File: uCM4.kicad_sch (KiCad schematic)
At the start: 74 parts, among them IC1 MAX17048G+, J1 Conn_02x07_Odd_Even, J10 USB_C_Receptacle, J11 SolderJumper_2_Open, J12 Conn_02x08_Odd_Even, J2 Micro_SD_Card_Det, J3 Conn_01x04, J4 Conn_01x04, J5 DummyJ, J6 DummyJ, J7 SolderJumper_2_Open, J8 Camera 0, J9 Camera 1, SW1 SW_DIP_x01, SW2 SW_DIP_x01, SW3 SW_Push, SW4 SW_Push, U1 BNO055, U18 RT9742GGJ5, U2 SN74LVC1G07DBVR, U3 TPD4EUSB30DQAR, U4 TPS61022, U5 BME690

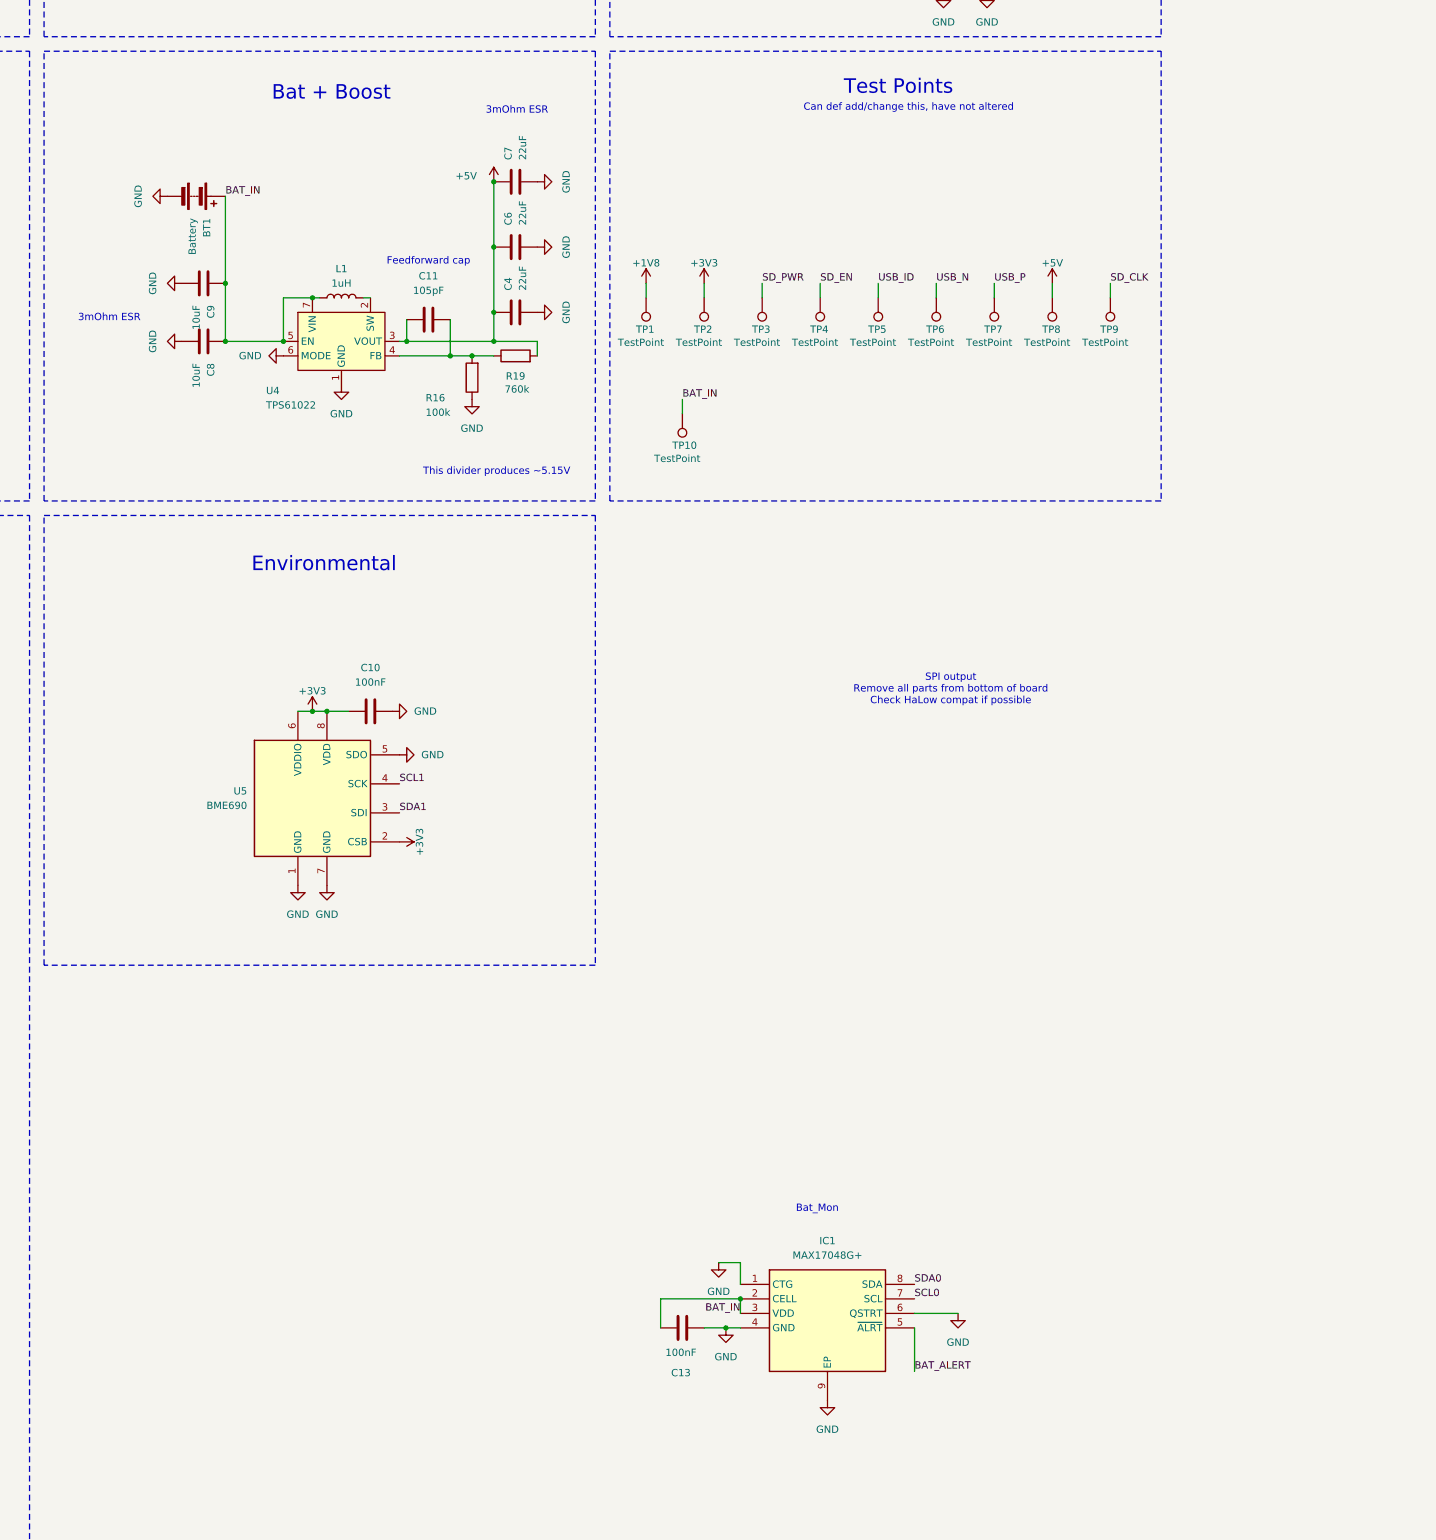
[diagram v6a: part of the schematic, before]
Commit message: Adding battery charging circuitry.
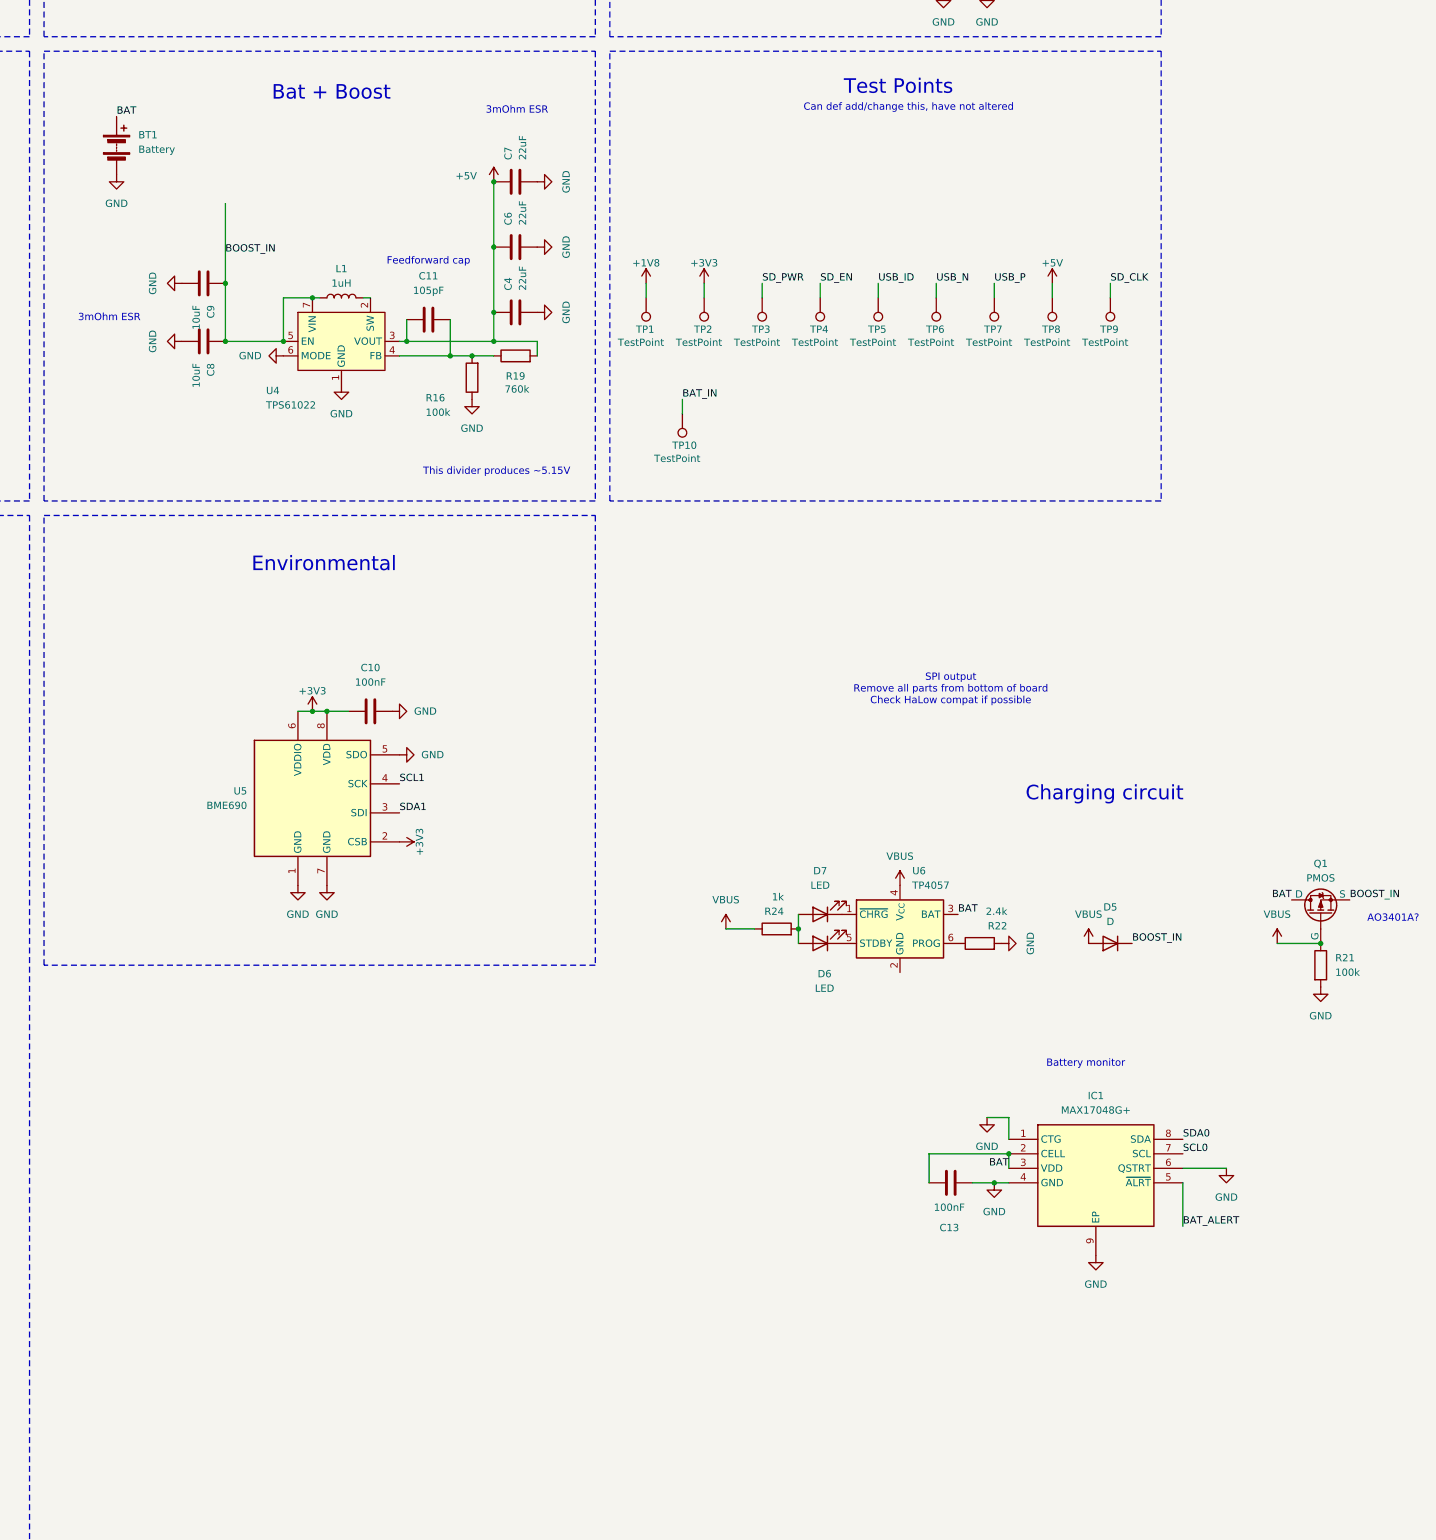
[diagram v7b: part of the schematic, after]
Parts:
- added D5: D, symbol Device:D
- added D6, D7: LED, symbol Device:LED
- added Q1: PMOS, symbol Simulation_SPICE:PMOS
- added R21: 100k, symbol Device:R
- added R22: 2.4k, symbol Device:R
- added R24: 1k, symbol Device:R
- added U6: TP4057, Package_TO_SOT_SMD:TSOT-23-6, symbol Battery_Management:TP4057
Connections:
- net BAT_IN: no longer BT1.1 (+), C13.1, C8.1, C9.1, IC1.2 (CELL), IC1.3 (VDD), L1.1, U4.5 (EN), U4.7 (VIN)
- net GND: now also R21.2, R22.2
- net VBUS: now also D5.2 (A), Q1.2 (G), R21.1, R24.1, U6.4 (V_{CC})
- new net: D6.2 (A), D7.2 (A), R24.2
- new net: R22.1, U6.6 (PROG)
- new net: D7.1 (K), U6.1 (~{CHRG})
- new net: D6.1 (K), U6.5 (STDBY)
- new net BAT: BT1.1 (+), C13.1, IC1.2 (CELL), IC1.3 (VDD), Q1.1 (D), U6.3 (BAT)
- new net BOOST_IN: C8.1, C9.1, D5.1 (K), L1.1, Q1.3 (S), U4.5 (EN), U4.7 (VIN)
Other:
- note added: "AO3401A?"
- note added: "Battery monitor"
- note added: "Charging circuit"
- note removed: "Bat_Mon"
- moved on the sheet: BT1, C13, IC1

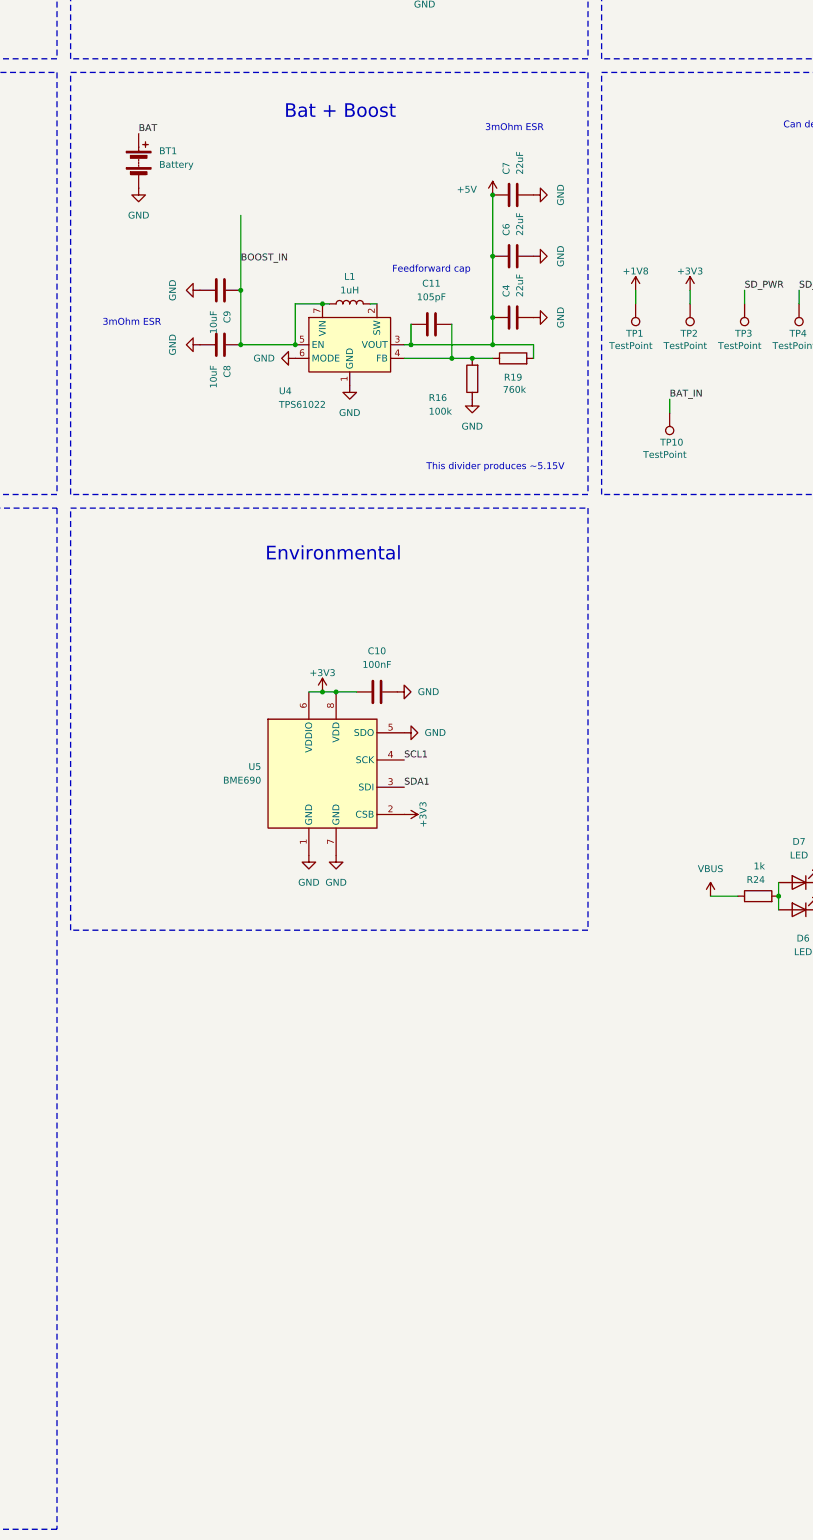
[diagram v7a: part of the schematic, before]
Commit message: Removing onboard environmental sensor.
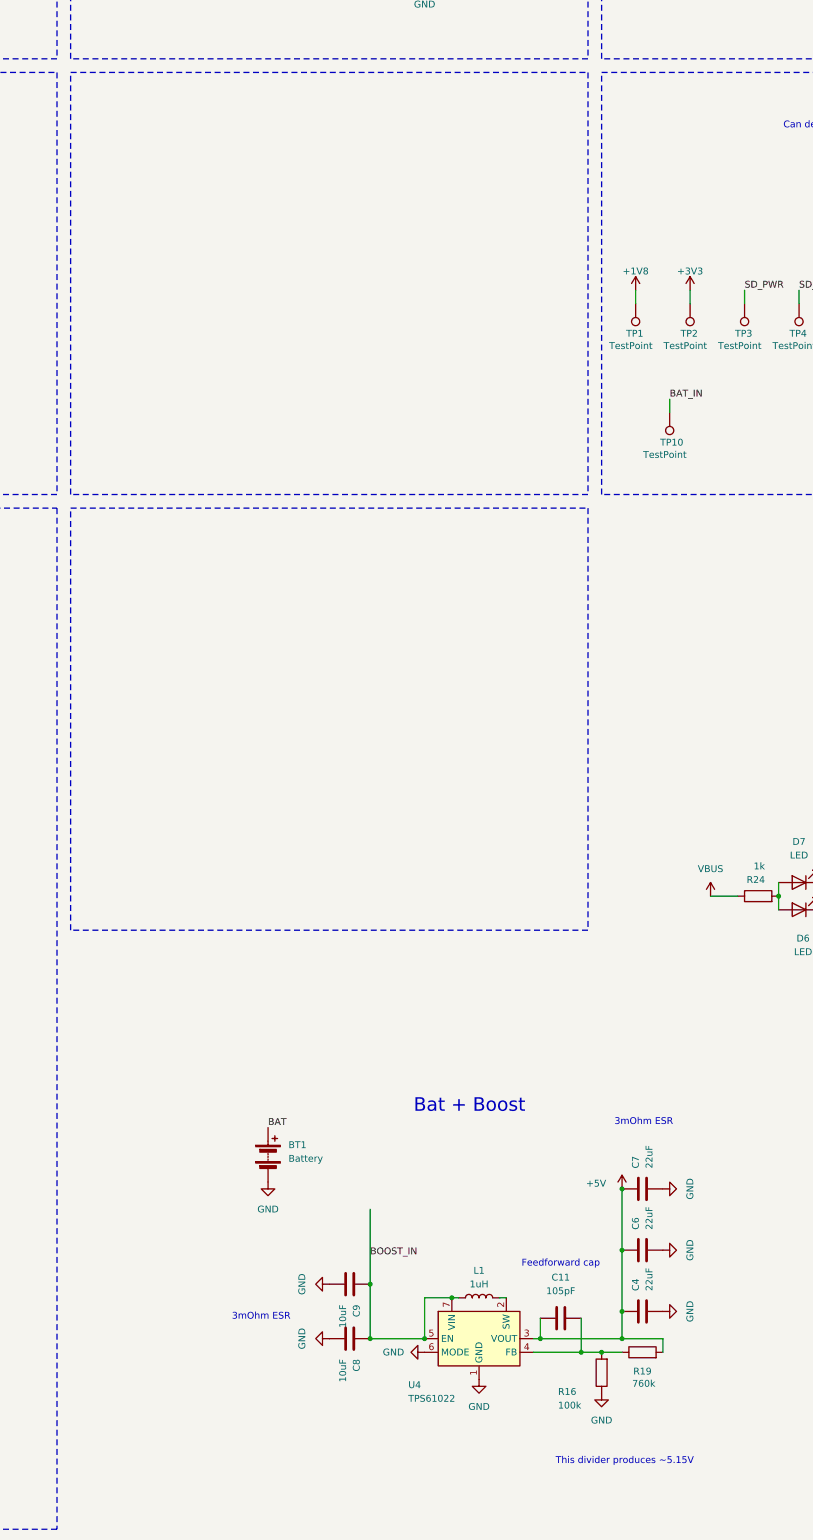
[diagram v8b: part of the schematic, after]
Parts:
- removed C10: 100nF, Capacitor_SMD:C_0603_1608Metric, symbol Device:C
- removed U5: BME690, Package_LGA:Bosch_LGA-8_3x3mm_P0.8mm_ClockwisePinNumbering, symbol Sensor:BME680
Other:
- note removed: "Environmental"
- moved on the sheet: BT1, C11, C4, C6, C7, C8, C9, L1, R16, R19, U4
